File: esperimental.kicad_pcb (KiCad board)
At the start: 2 copper layers, 30 x 30.8 mm, 10 parts, among them P1 CONN_01X01, P2 CONN_01X01

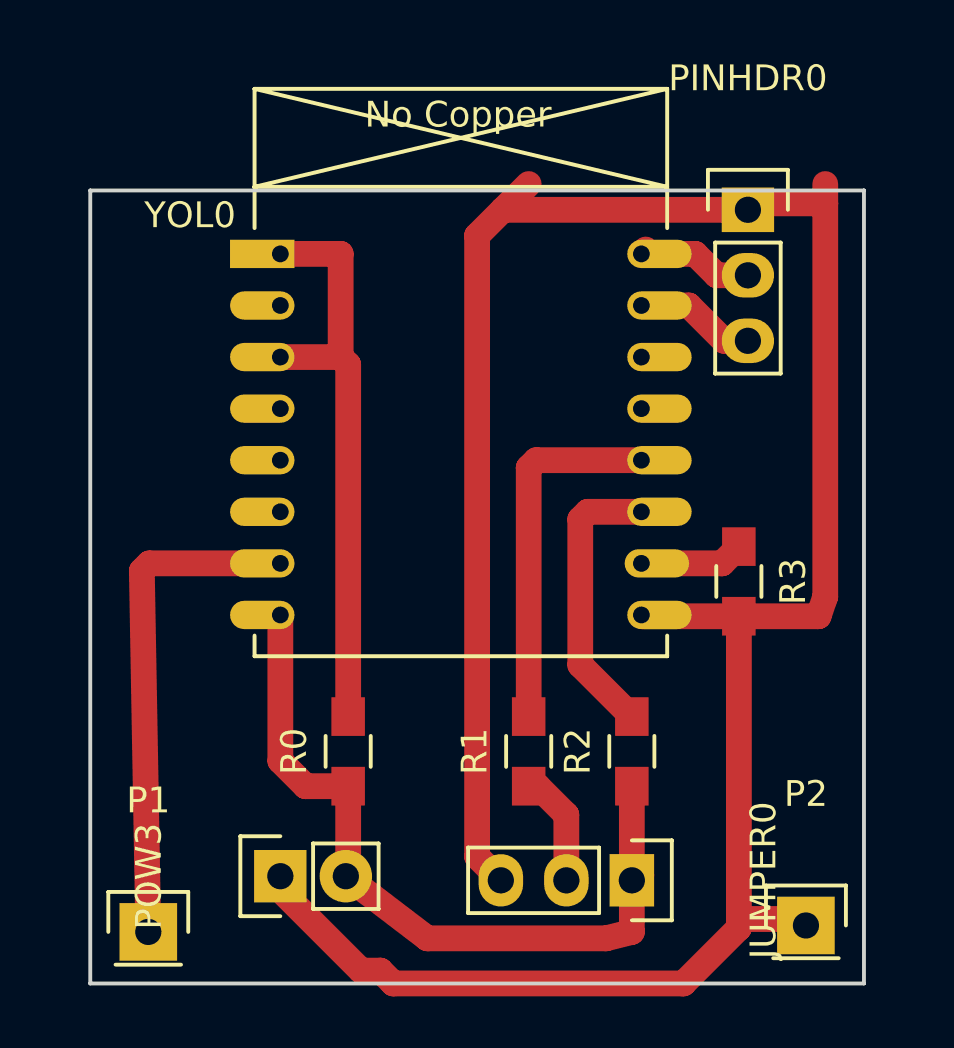
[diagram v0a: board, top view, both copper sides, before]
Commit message: first draft of probably millable board
* adapt schematic slightly for easier production
* fix ESP8266 footprint to no longer include unnecessary drill holes
* add a ground fill
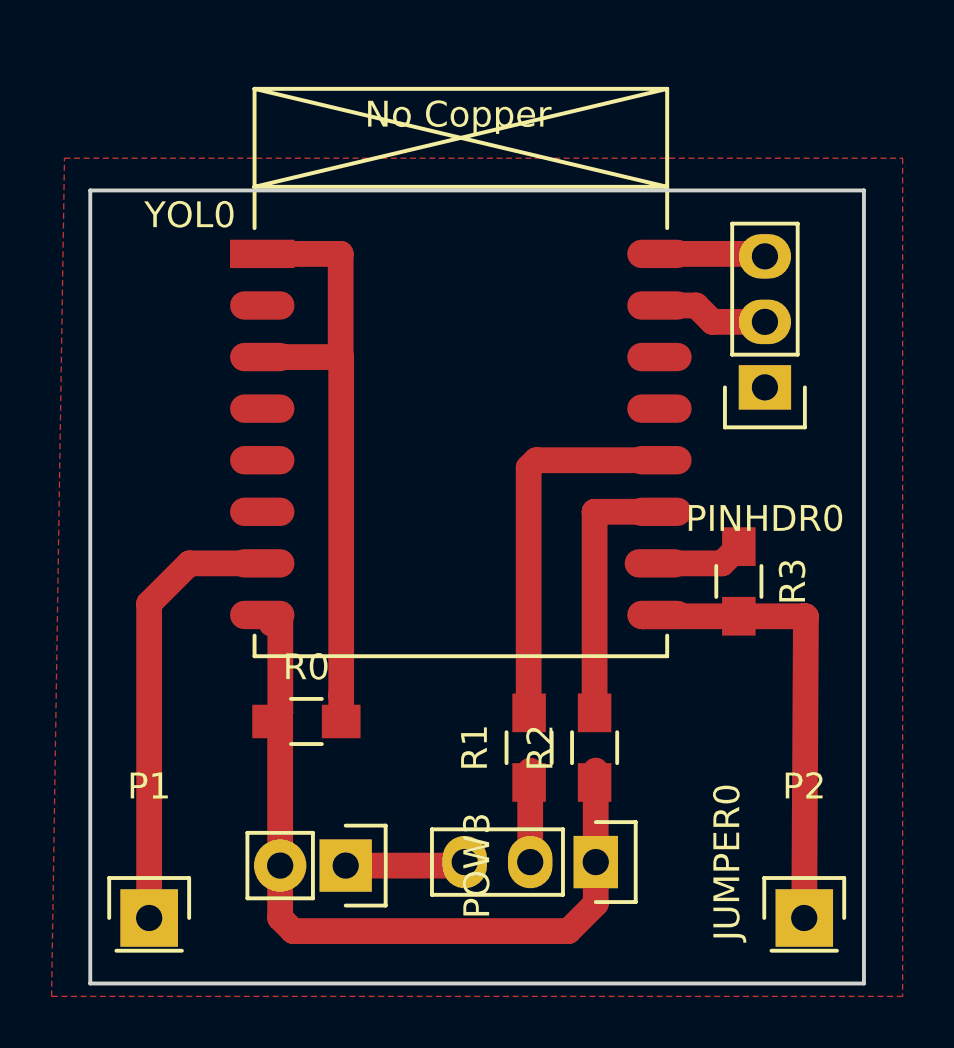
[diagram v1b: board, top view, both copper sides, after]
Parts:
- YOL0: footprint ESP8266:ESP-07v2 -> ESP8266SMD:ESP-07v2_smd
- moved PINHDR0 6.92 mm to (183.2, 97.9), turned to 180 degrees
- moved POW3 2.57 mm to (166.9, 116.4), turned to 270 degrees
- moved R0 1.99 mm to (165.4, 110.8), turned to 0 degrees
- moved JUMPER0 1.57 mm to (176.6, 116.3)
- moved R2 1.45 mm to (176.6, 111.9)
- moved P1 0.54 mm to (159.3, 118.5)
- moved P2 0.30 mm to (184.7, 118.5)
- moved R1 0.14 mm to (174.0, 111.9)
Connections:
- YOL0 pad 13: Net-(YOL0-Pad13) -> (no net)
- YOL0 pad 14: Net-(YOL0-Pad14) -> (no net)
- YOL0 pad 15: Net-(PINHDR0-Pad3) -> Net-(PINHDR0-Pad2)
- YOL0 pad 16: Net-(PINHDR0-Pad2) -> Net-(PINHDR0-Pad3)
- YOL0 pad 2: Net-(YOL0-Pad2) -> (no net)
- YOL0 pad 4: Net-(YOL0-Pad4) -> (no net)
- YOL0 pad 5: Net-(YOL0-Pad5) -> (no net)
- YOL0 pad 6: Net-(YOL0-Pad6) -> (no net)
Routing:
- net GND: track 100.3 -> 23.3 mm
- net +3V3: track 29.9 -> 32.0 mm
- net Net-(P1-Pad1): track 19.5 -> 17.9 mm
- net Net-(R2-Pad2): track 11.0 -> 9.61 mm
- net Net-(JUMPER0-Pad2): track 4.46 -> 3.61 mm
- added copper zone on F.Cu, net GND
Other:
- net class Default: clearance 0.5 -> 0.6
- rule trace_clearance: 0.5 -> 0.6

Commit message: add entropia text
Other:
- board text added: "entropia"
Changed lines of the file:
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@@
     (links 18)
     (no_connects 0)
-    (area 156.924999 90.174999 187.075001 121.075001)
+    (area 153.775667 85.434999 190.192334 121.936333)
     (thickness 1.6)
-    (drawings 4)
+    (drawings 5)
     (tracks 51)
     (zones 0)
@@
     )
   )
+  (gr_text entropia (at 158.776 95.6 270) (layer F.Cu)
+    (effects (font (size 1.5 1.5) (thickness 0.3)))
+  )
   (gr_line (start 157 90.25) (end 157 121) (angle 90) (layer Edge.Cuts) (width 0.15))
